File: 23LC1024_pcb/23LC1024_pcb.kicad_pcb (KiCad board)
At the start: 2 copper layers, 9 parts, among them J1 Conn_01x06_Male_JA, J2 Conn_01x06_Male_JB, U1 23LC1024-I/P, U2 AP2141SG-13

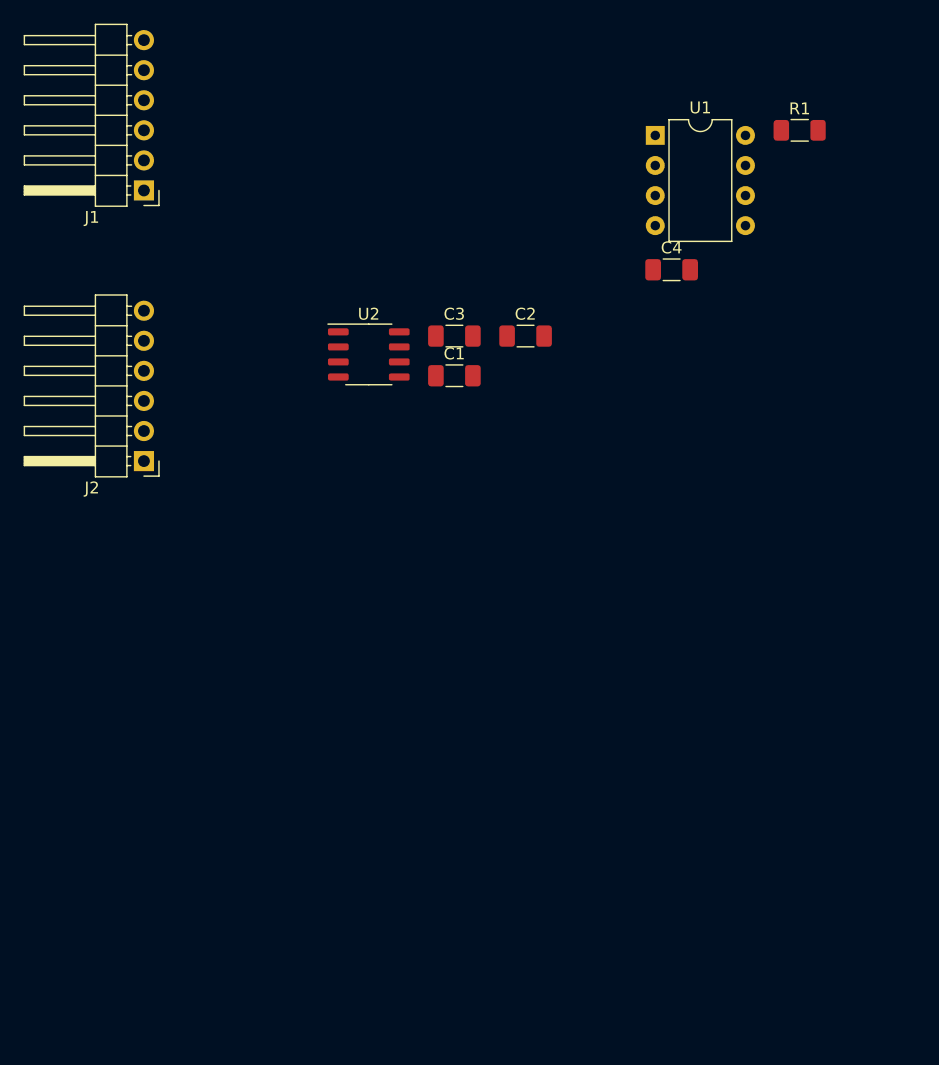
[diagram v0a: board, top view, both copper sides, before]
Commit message: 23LC1024 PCB: Finish routing
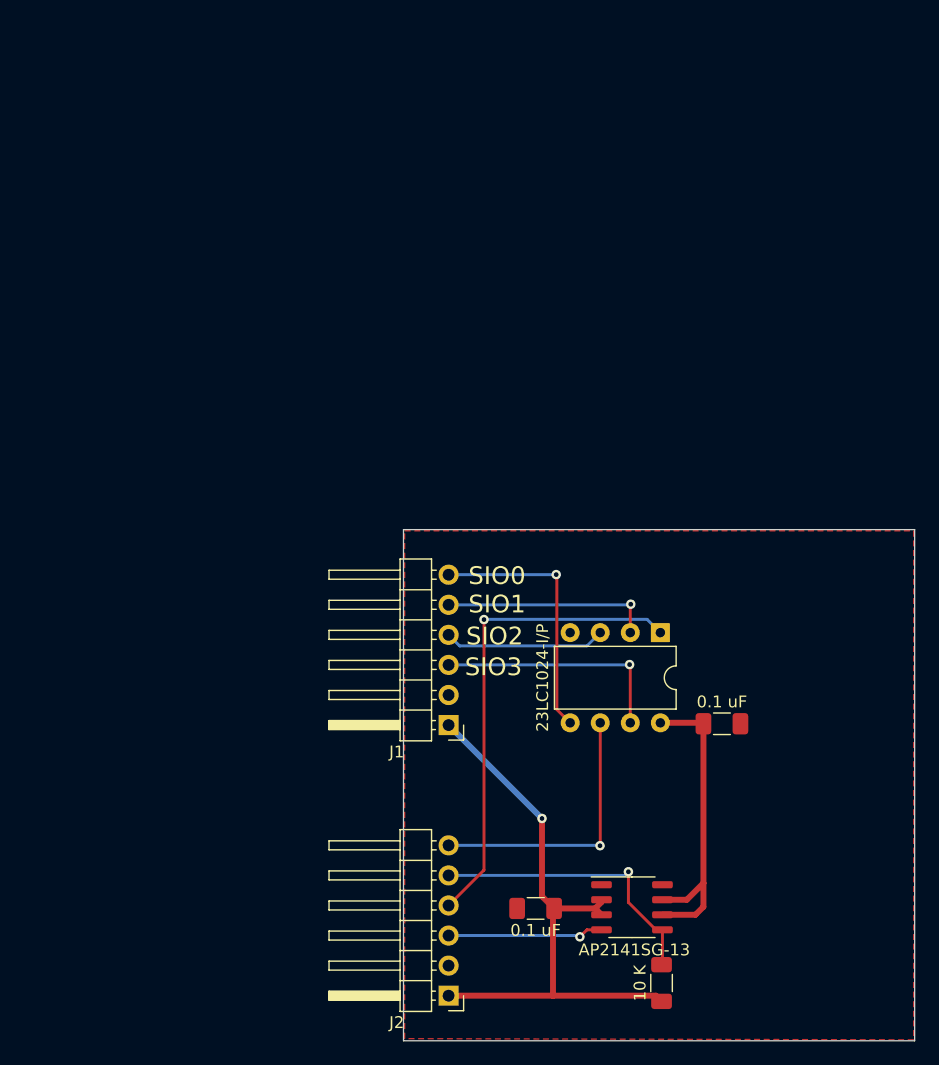
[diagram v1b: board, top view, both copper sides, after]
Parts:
- removed the C1 at (104.3, 87.0)
- removed C4: 120 uF, Capacitor_SMD:C_1206_3216Metric_Pad1.33x1.80mm_HandSolder
- moved R1 73.0 mm to (121.8, 138.3), turned to -90 degrees
- moved J1 52.0 mm to (103.8, 116.5)
- moved J2 52.0 mm to (103.8, 139.4)
- moved U2 51.7 mm to (119.3, 131.9)
- moved C1 48.4 mm to (111.2, 132.0)
- moved U1 42.0 mm to (121.7, 108.7), turned to -90 degrees
- moved C2 39.8 mm to (126.9, 116.4), turned to 180 degrees
- renumbered C2 to C1, C3 to C2
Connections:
- C1 pad 2: +3V3 -> BASYS3V3
- J1 pad 1: /SIO0 -> BASYS3V3
- J1 pad 2: /SIO1 -> GND
- J1 pad 3: /SIO2 -> /SIO3
- J1 pad 4: /SIO3 -> /SIO2
- J1 pad 5: GND -> /SIO1
- J1 pad 6: +3V3 -> /SIO0
- J2 pad 1: /CLK -> BASYS3V3
- J2 pad 2: /FLG -> GND
- J2 pad 3: /CS -> /EN
- J2 pad 4: /EN -> /CS
- J2 pad 5: GND -> /FLG
- J2 pad 6: +3V3 -> /CLK
- R1 pad 2: +3V3 -> BASYS3V3
- U2 pad 2: +3V3 -> BASYS3V3
- U2 pad 3: +3V3 -> BASYS3V3
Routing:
- net BASYS3V3: track 0.00 -> 50.0 mm, vias 0 -> 1
- net /CS: track 0.00 -> 40.8 mm, vias 0 -> 1
- net +3V3: track 0.00 -> 26.9 mm
- net /FLG: track 0.00 -> 24.7 mm, vias 0 -> 1
- net /CLK: track 0.00 -> 23.2 mm, vias 0 -> 1
- net /SIO0: track 0.00 -> 22.1 mm, vias 0 -> 1
- net /SIO3: track 0.00 -> 20.2 mm, vias 0 -> 1
- net /SIO1: track 0.00 -> 17.8 mm, vias 0 -> 1
- net /SIO2: track 0.00 -> 13.7 mm
- net /EN: track 0.00 -> 13.2 mm, vias 0 -> 1
- added copper zone on F.Cu, net GND
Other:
- board outline added: 43.2 x 43.2 mm
- board text added: "SIO0"
- board text added: "SIO1"
- board text added: "SIO2"
- board text added: "SIO3"

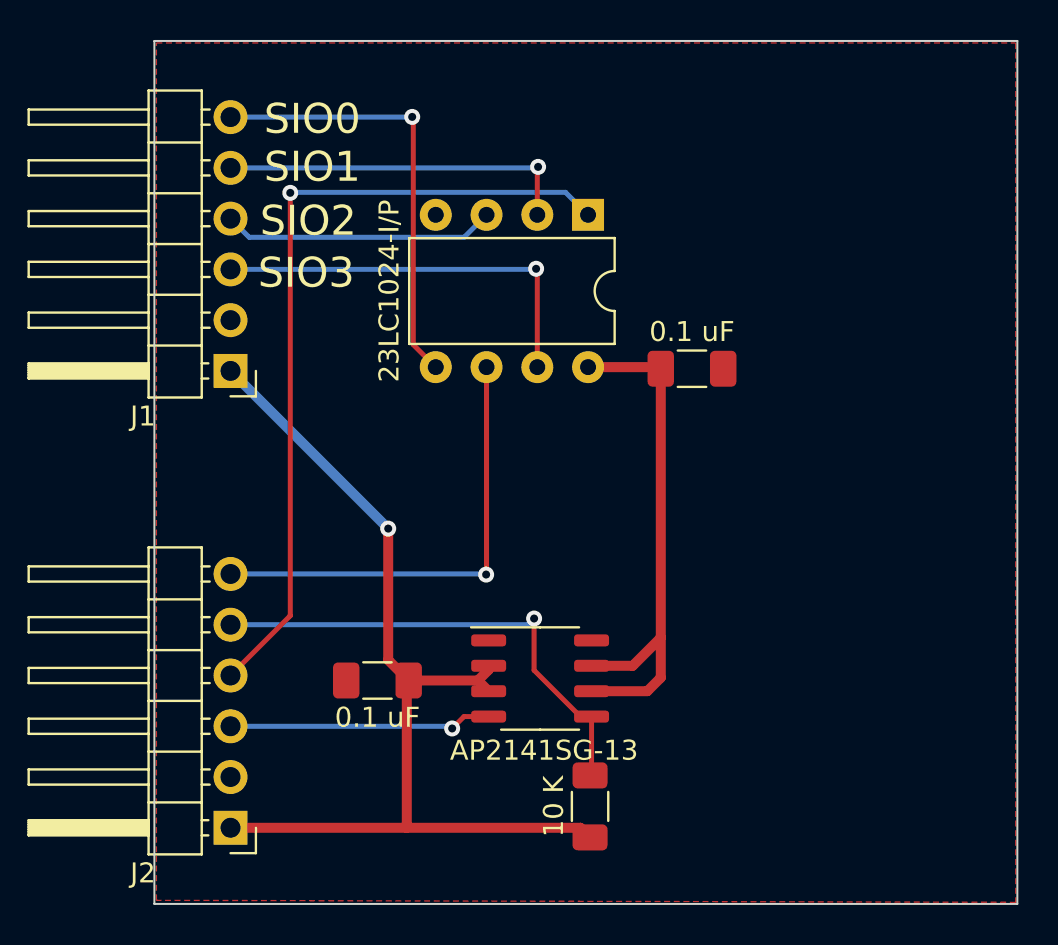
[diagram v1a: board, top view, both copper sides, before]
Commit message: 23LC1024 PCB: Rework to add three
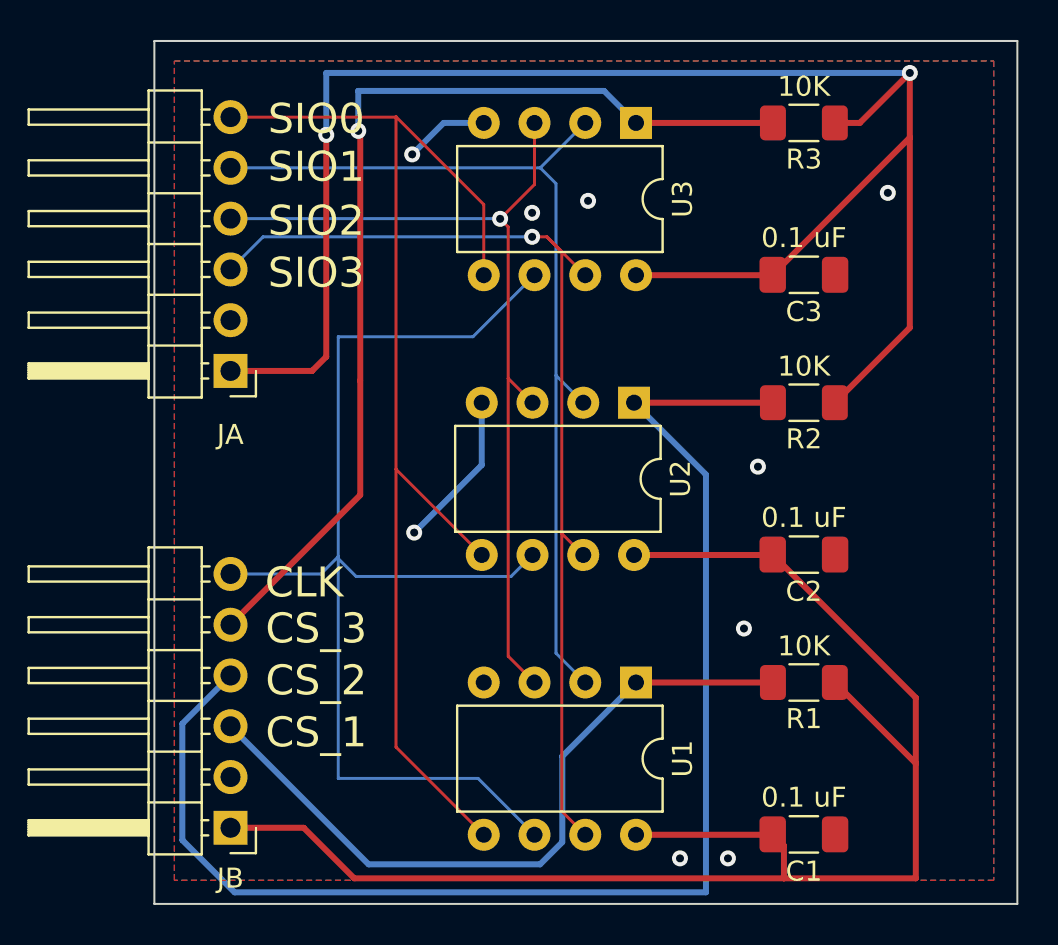
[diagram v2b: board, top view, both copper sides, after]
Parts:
- added C3: 0.1 uF, Capacitor_SMD:C_1206_3216Metric_Pad1.33x1.80mm_HandSolder, F.Cu at (132.5, 111.7)
- added R2: 10K, Resistor_SMD:R_1206_3216Metric_Pad1.30x1.75mm_HandSolder, F.Cu at (132.5, 118.1)
- added R3: 10K, Resistor_SMD:R_1206_3216Metric_Pad1.30x1.75mm_HandSolder, F.Cu at (132.5, 104.1)
- added U3: 23LC1024-I/P, Package_DIP:DIP-8_W7.62mm, F.Cu at (124.1, 104.1)
- R1: value 10 K -> 10K
- U2: value AP2141SG-13 -> 23LC1024-I/P; footprint Package_SO:SO-8_3.9x4.9mm_P1.27mm -> Package_DIP:DIP-8_W7.62mm
- moved U1 23.5 mm to (124.1, 132.1)
- moved C1 22.7 mm to (132.5, 139.7), turned to 180 degrees
- moved U2 14.6 mm to (124.0, 118.1), turned to -90 degrees
- moved R1 12.4 mm to (132.5, 132.1), turned to 180 degrees
- moved C2 10.9 mm to (132.5, 125.7)
- renumbered J1 to JA, J2 to JB
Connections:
- C2 pad 2: +3V3 -> BASYS3V3
- JB pad 3: /EN -> /CS_1
- JB pad 4: /CS -> /CS_2
- JB pad 5: /FLG -> /CS_3
- R1 pad 1: /FLG -> BASYS3V3
- R1 pad 2: BASYS3V3 -> /CS_1
- U1 pad 1: /CS -> /CS_1
- U1 pad 8: +3V3 -> BASYS3V3
- U2 pad 1: GND -> /CS_2
- U2 pad 2: BASYS3V3 -> /SIO1
- U2 pad 3: BASYS3V3 -> /SIO2
- U2 pad 4: /EN -> GND
- U2 pad 5: /FLG -> /SIO0
- U2 pad 6: +3V3 -> /CLK
- U2 pad 7: +3V3 -> /SIO3
- U2 pad 8: unconnected-(U2-Pad8) -> BASYS3V3
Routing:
- net BASYS3V3: track 50.0 -> 164.3 mm, vias 1 -> 2
- net /CS_2: track 0.00 -> 69.5 mm
- net /CS_3: track 0.00 -> 50.9 mm, vias 0 -> 1
- net /CS: track 40.8 -> 0.00 mm, vias 1 -> 0
- net /SIO0: track 22.1 -> 61.8 mm, vias 1 -> 0
- net /CLK: track 23.2 -> 60.5 mm, vias 1 -> 0
- net /CS_1: track 0.00 -> 36.3 mm
- net /SIO3: track 20.2 -> 51.5 mm
- net /SIO2: track 13.7 -> 44.6 mm, vias 0 -> 1
- net /SIO1: track 17.8 -> 47.3 mm, vias 1 -> 0
- net +3V3: track 26.9 -> 0.00 mm
- net /FLG: track 24.7 -> 0.00 mm, vias 1 -> 0
- net /EN: track 13.2 -> 0.00 mm, vias 1 -> 0
- net GND: track 0.00 -> 12.1 mm, vias 0 -> 9
- added copper zone on B.Cu, net GND
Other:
- board text added: "CLK"
- board text added: "CS_1"
- board text added: "CS_2"
- board text added: "CS_3"
